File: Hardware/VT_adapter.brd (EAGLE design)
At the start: 40 x 40 mm, 14 parts

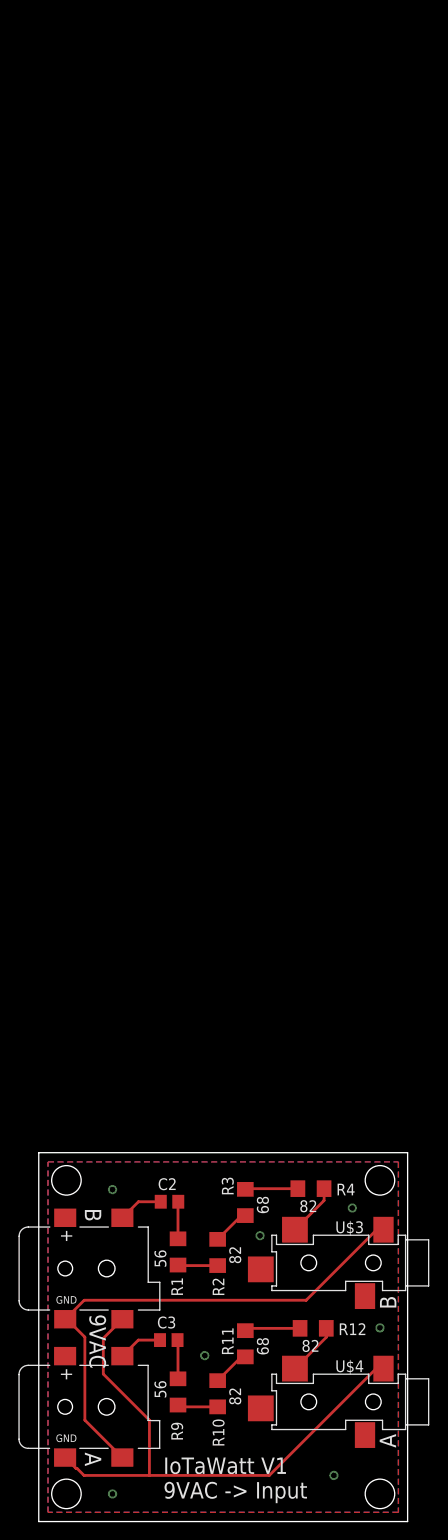
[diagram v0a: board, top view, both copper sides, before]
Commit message: V2 adapter board
Use of this adapter requires removing burden resistor(s) from IoTaWatt.
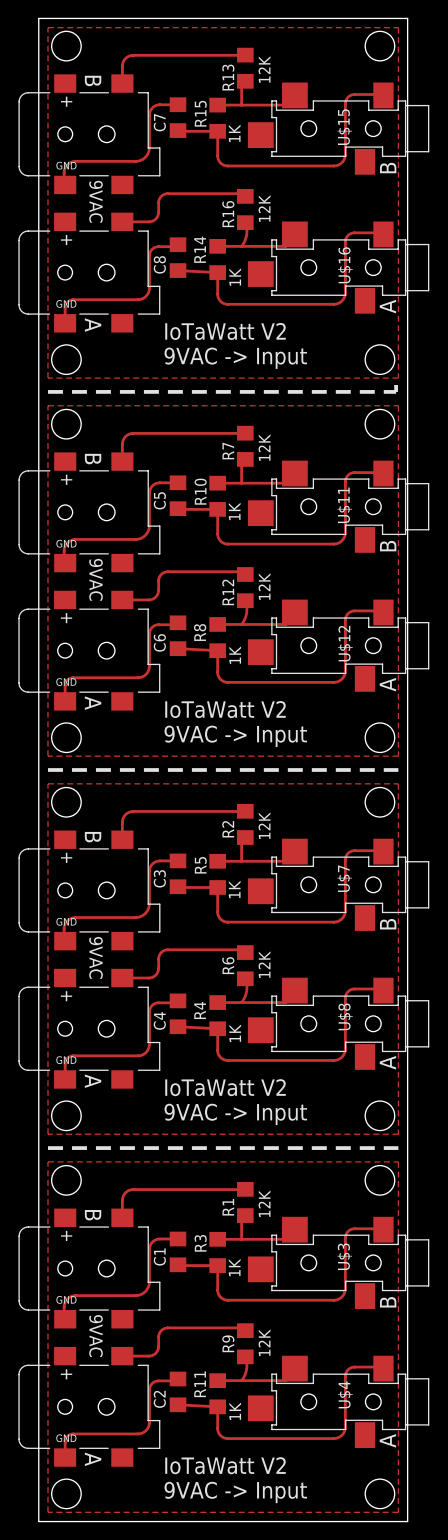
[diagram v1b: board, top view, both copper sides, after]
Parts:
- added C1, C4, C5, C6, C7, C8: 10uf, adafruit:C1206
- added R13, R16, R6, R7: 12K, resistor:R1206
- added R14, R15, R5, R8: 1K, resistor:R1206
- added U$10, U$13, U$14, U$5, U$6, U$9: 2.1MMJACKSMT, IotaWatt_parts:DCJACK_2MM_SMT
- added U$11, U$12, U$15, U$16, U$7, U$8: STEREO_SMD, IotaWatt_parts:STEREO_SMT
- C2, C3: device resistor:C0805 -> adafruit:C1206
- R1, R9: value 56 -> 12K
- R10, R4: value 82 -> 1K
- R11, R3: value 68 -> 1K
- R12, R2: value 82 -> 12K
- moved R10 97.3 mm to (19.4, 111.2), turned to 270 degrees
- moved R12 80.7 mm to (22.4, 101.3), turned to 270 degrees
- moved C3 50.6 mm to (15.1, 70.2), turned to 270 degrees
- moved R2 46.5 mm to (22.4, 75.6), turned to 270 degrees
- moved R4 21.3 mm to (19.4, 54.9), turned to 90 degrees
- moved C2 20.6 mm to (15.1, 14.1), turned to 270 degrees
- moved R1 9.06 mm to (22.4, 34.6)
- moved R9 8.97 mm to (22.4, 19.3)
- moved R11 6.19 mm to (19.4, 13.9)
- moved R3 6.19 mm to (19.4, 29.2), turned to 270 degrees
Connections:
- new net N$15: R6.1, U$6.PWR2
- new net N$16: R2.2, R5.1, U$7.P$2
- new net N$17: R12.2, R8.2, U$12.P$2
- new net N$18: C6.2, R8.1, U$12.P$1
- new net N$19: C5.2, R10.2, U$11.P$1
- new net N$20: C5.1, U$9.GND
- new net N$21: R7.1, U$9.PWR2
- new net N$22: C6.1, U$10.GND
- new net N$23: R12.1, U$10.PWR2
- new net N$24: R10.1, R7.2, U$11.P$2
- new net N$25: R14.2, R16.2, U$16.P$2
- new net N$26: C8.2, R14.1, U$16.P$1
- new net N$27: C7.2, R15.2, U$15.P$1
- new net N$28: C7.1, U$13.GND
- new net N$29: R13.1, U$13.PWR2
- new net N$30: C8.1, U$14.GND
- new net N$31: R16.1, U$14.PWR2
- new net N$32: R13.2, R15.1, U$15.P$2
- net N$1: now also C1.2, R3.2, U$3.P$1; no longer C2.1, U$1.PWR2
- net N$10: now also C3.1, U$5.GND; no longer R11.2, R12.1
- net N$11: now also R11.2, R9.2; no longer R12.2
- net N$12: now also C2.2, R11.1; no longer U$1.GNDBREAK, U$2.GND
- net N$13: now also R2.1, U$5.PWR2; no longer C2.2, R1.1
- net N$14: now also C4.1, U$6.GND; no longer C3.2, R9.1
- net N$2: now also R3.1, U$3.P$2; no longer R2.1
- net N$3: now also C1.1, U$1.GND; no longer R2.2, R3.1
- net N$4: now also C2.1, U$2.GND; no longer R3.2, R4.1
- net N$5: now also R6.2, U$8.P$2; no longer U$3.P$2
- net N$6: now also R1.1, U$1.PWR2; no longer U$1.GND, U$2.GNDBREAK, U$3.P$1
- net N$7: now also R9.1; no longer C3.1
- net N$8: now also C4.2, R4.1, U$8.P$1; no longer R10.1, R9.2
- net N$9: now also C3.2, R5.2, U$7.P$1; no longer R10.2, R11.1
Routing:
- net N$6: track 56.2 -> 15.7 mm
- net N$27: track 0.00 -> 32.6 mm
- net N$19: track 0.00 -> 32.6 mm
- net N$18: track 0.00 -> 31.6 mm, vias 1 -> 0
- net N$26: track 0.00 -> 31.6 mm
- net N$9: track 4.07 -> 32.6 mm
- net N$12: track 60.0 -> 31.6 mm
- net N$1: track 4.88 -> 32.6 mm
- net N$8: track 4.38 -> 31.6 mm
- net N$30: track 0.00 -> 19.7 mm
- net N$22: track 0.00 -> 19.7 mm, vias 1 -> 0
- net N$20: track 0.00 -> 18.8 mm, vias 1 -> 0
- net N$28: track 0.00 -> 18.8 mm
- net N$21: track 0.00 -> 15.7 mm, vias 1 -> 0
- net N$29: track 0.00 -> 15.7 mm
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- added copper zone on layer 1, net GND1
- added copper zone on layer 1, net GND2
- added copper zone on layer 1, net GND3
- removed copper zone on layer 16, net GND
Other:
- board size 40 x 40 mm -> 40 x 163 mm
- board text added: "IoTaWatt V2 9VAC -> Input"
- board text removed: "IoTaWatt V1 9VAC -> Input"
